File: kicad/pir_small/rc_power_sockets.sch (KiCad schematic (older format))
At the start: 26 parts, among them IC1 ATTINY85, J1 PIR, J2 433MHZ, P1 ICSP, P2 ALT_PWR, Q1 NMOS, Q2 PMOS, SW1 SWITCH_INV, U1 MCP1755ST-3302E/DB

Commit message: Changed layout
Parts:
- removed RV1: POT, Pin_Headers:Pin_Header_Straight_1x03, symbol POT-RESCUE-rc_power_sockets
- added P3, P4: CONN_01X01, theapi_footprints:SMD_PAD, symbol CONN_01X01
- D1, D2, D3: footprint theapi_footprints:SOD-123-Schottky -> theapi_footprints:SOD-123-handsolder
- IC1: footprint theapi_footprints:SOIC-8-N-hand-sold -> theapi_footprints:SOIC-8-N-handsolder
- P2: footprint Pin_Headers:Pin_Header_Straight_1x02 -> Socket_Strips:Socket_Strip_Straight_1x02
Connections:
- net 3.3v: now also P4.1 (P1)
- net ADC3: now also P3.1 (P1)
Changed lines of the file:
@@
 F 0 "IC1" H 5100 5700 50  0000 C CNN
 F 1 "ATTINY85" H 7250 4900 50  0000 C CNN
-F 2 "theapi_footprints:SOIC-8-N-hand-sold" H 7200 5300 50  0000 C CIN
+F 2 "theapi_footprints:SOIC-8-N-handsolder" H 7200 5300 50  0000 C CIN
 F 3 "" H 6250 5300 50  0000 C CNN
 	1    6250 5300
 	1    0    0    -1
 $EndComp
-$Comp
-L POT-RESCUE-rc_power_sockets RV1
-U 1 1 56E809B9
-P 9350 5050
-F 0 "RV1" H 9350 4970 50  0000 C CNN
-F 1 "POT" H 9350 5050 50  0000 C CNN
-F 2 "Pin_Headers:Pin_Header_Straight_1x03" H 9350 5050 50  0001 C CNN
-F 3 "" H 9350 5050 50  0000 C CNN
-	1    9350 5050
-	0    -1   -1   0
-$EndComp
-$Comp
-L GND #PWR08
-U 1 1 56E80AFC
-P 9350 5200
-F 0 "#PWR08" H 9350 4950 50  0001 C CNN
-F 1 "GND" H 9350 5050 50  0000 C CNN
-F 2 "" H 9350 5200 50  0000 C CNN
-F 3 "" H 9350 5200 50  0000 C CNN
-	1    9350 5200
-	1    0    0    -1
-$EndComp
 Text Label 4300 5350 0    60   ~ 0
-ADC3
-Text Label 8900 5050 0    60   ~ 0
 ADC3
 $Comp
@@
 Connection ~ 8250 5050
 Wire Wire Line
-	9200 5050 8900 5050
-Wire Wire Line
-	4900 5350 4300 5350
+	4900 5350 3600 5350
 Connection ~ 6550 3450
 Wire Wire Line
@@
 F 0 "D1" H 4150 3000 50  0000 C CNN
 F 1 "D_Schottky" V 4150 2600 50  0000 C CNN
-F 2 "theapi_footprints:SOD-123-Schottky" H 4150 2900 50  0001 C CNN
+F 2 "theapi_footprints:SOD-123-handsolder" H 4150 2900 50  0001 C CNN
 F 3 "" H 4150 2900 50  0000 C CNN
 	1    4150 2900
@@
 F 0 "D2" H 4150 3350 50  0000 C CNN
 F 1 "D_Schottky" V 4150 3750 50  0000 C CNN
-F 2 "theapi_footprints:SOD-123-Schottky" H 4150 3450 50  0001 C CNN
+F 2 "theapi_footprints:SOD-123-handsolder" H 4150 3450 50  0001 C CNN
 F 3 "" H 4150 3450 50  0000 C CNN
 	1    4150 3450
@@
 F 0 "D3" H 5550 1550 50  0000 C CNN
 F 1 "D_Schottky" V 5550 1950 50  0000 C CNN
-F 2 "theapi_footprints:SOD-123-Schottky" H 5550 1650 50  0001 C CNN
+F 2 "theapi_footprints:SOD-123-handsolder" H 5550 1650 50  0001 C CNN
 F 3 "" H 5550 1650 50  0000 C CNN
 	1    5550 1650
@@
 Wire Wire Line
 	4100 5950 4100 5850
-Wire Wire Line
-	9350 4900 9350 4750
 Wire Wire Line
 	9350 4750 8600 4750
@@
 	2150 5050 1900 5050
 $Comp
-L GND #PWR09
+L GND #PWR08
 U 1 1 56F5DB12
 P 1500 5200
-F 0 "#PWR09" H 1500 4950 50  0001 C CNN
+F 0 "#PWR08" H 1500 4950 50  0001 C CNN
 F 1 "GND" H 1500 5050 50  0000 C CNN
 F 2 "" H 1500 5200 50  0000 C CNN
@@
 Connection ~ 7350 4050
 $Comp
-L GND #PWR010
+L GND #PWR09
 U 1 1 56F7F83F
 P 8600 1050
-F 0 "#PWR010" H 8600 800 50  0001 C CNN
+F 0 "#PWR09" H 8600 800 50  0001 C CNN
 F 1 "GND" H 8600 900 50  0000 C CNN
 F 2 "" H 8600 1050 50  0000 C CNN
@@
 F 0 "P2" H 8800 1150 50  0000 C CNN
 F 1 "ALT_PWR" H 9050 1000 50  0000 C CNN
-F 2 "Pin_Headers:Pin_Header_Straight_1x02" H 8800 1000 50  0001 C CNN
+F 2 "Socket_Strips:Socket_Strip_Straight_1x02" H 8800 1000 50  0001 C CNN
 F 3 "" H 8800 1000 50  0000 C CNN
 	1    8800 1000
@@
 $EndComp
 $Comp
-L GND #PWR011
+L GND #PWR010
 U 1 1 56F8174A
 P 1100 2100
-F 0 "#PWR011" H 1100 1850 50  0001 C CNN
+F 0 "#PWR010" H 1100 1850 50  0001 C CNN
 F 1 "GND" H 1100 1950 50  0000 C CNN
 F 2 "" H 1100 2100 50  0000 C CNN
@@
 $EndComp
 $Comp
-L GND #PWR012
+L GND #PWR011
 U 1 1 56F817AF
 P 1550 2100
-F 0 "#PWR012" H 1550 1850 50  0001 C CNN
+F 0 "#PWR011" H 1550 1850 50  0001 C CNN
 F 1 "GND" H 1550 1950 50  0000 C CNN
 F 2 "" H 1550 2100 50  0000 C CNN
@@
 	6700 850  6550 850
 $Comp
-L GND #PWR013
+L GND #PWR012
 U 1 1 56FBCCBF
 P 6550 1050
-F 0 "#PWR013" H 6550 800 50  0001 C CNN
+F 0 "#PWR012" H 6550 800 50  0001 C CNN
 F 1 "GND" H 6550 900 50  0000 C CNN
 F 2 "" H 6550 1050 50  0000 C CNN
@@
 $EndComp
 $Comp
-L GND #PWR014
+L GND #PWR013
 U 1 1 5722073A
 P 1100 2750
-F 0 "#PWR014" H 1100 2500 50  0001 C CNN
+F 0 "#PWR013" H 1100 2500 50  0001 C CNN
 F 1 "GND" H 1100 2600 50  0000 C CNN
 F 2 "" H 1100 2750 50  0000 C CNN
@@
 $EndComp
 $Comp
-L GND #PWR015
+L GND #PWR014
 U 1 1 57220740
 P 1550 2750
-F 0 "#PWR015" H 1550 2500 50  0001 C CNN
+F 0 "#PWR014" H 1550 2500 50  0001 C CNN
 F 1 "GND" H 1550 2600 50  0000 C CNN
 F 2 "" H 1550 2750 50  0000 C CNN
@@
 	1    0    0    -1
 $EndComp
+$Comp
+L CONN_01X01 P4
+U 1 1 57266A41
+P 9550 4750
+F 0 "P4" H 9550 4850 50  0000 C CNN
+F 1 "CONN_01X01" V 9650 4750 50  0000 C CNN
+F 2 "theapi_footprints:SMD_PAD" H 9550 4750 50  0001 C CNN
+F 3 "" H 9550 4750 50  0000 C CNN
+	1    9550 4750
+	1    0    0    -1
+$EndComp
+$Comp
+L CONN_01X01 P3
+U 1 1 57266AA6
+P 3400 5350
+F 0 "P3" H 3400 5450 50  0000 C CNN
+F 1 "CONN_01X01" V 3500 5350 50  0000 C CNN
+F 2 "theapi_footprints:SMD_PAD" H 3400 5350 50  0001 C CNN
+F 3 "" H 3400 5350 50  0000 C CNN
+	1    3400 5350
+	-1   0    0    1
+$EndComp
 $EndSCHEMATC

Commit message: Silkscreen
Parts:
- P3, P4: footprint theapi_footprints:SMD_PAD -> Pin_Headers:Pin_Header_Straight_1x01
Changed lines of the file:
@@
+$EndComp
+$Comp
+L CONN_01X01 P3
+U 1 1 57266AA6
+P 3400 5350
+F 0 "P3" H 3400 5450 50  0000 C CNN
+F 1 "CONN_01X01" V 3500 5350 50  0000 C CNN
+F 2 "Pin_Headers:Pin_Header_Straight_1x01" H 3400 5350 50  0001 C CNN
+F 3 "" H 3400 5350 50  0000 C CNN
+	1    3400 5350
+	-1   0    0    1
 $EndComp
 $Comp
@@
 F 0 "P4" H 9550 4850 50  0000 C CNN
 F 1 "CONN_01X01" V 9650 4750 50  0000 C CNN
-F 2 "theapi_footprints:SMD_PAD" H 9550 4750 50  0001 C CNN
+F 2 "Pin_Headers:Pin_Header_Straight_1x01" H 9550 4750 50  0001 C CNN
 F 3 "" H 9550 4750 50  0000 C CNN
 	1    9550 4750
 	1    0    0    -1
 $EndComp
-$Comp
-L CONN_01X01 P3
-U 1 1 57266AA6
-P 3400 5350
-F 0 "P3" H 3400 5450 50  0000 C CNN
-F 1 "CONN_01X01" V 3500 5350 50  0000 C CNN
-F 2 "theapi_footprints:SMD_PAD" H 3400 5350 50  0001 C CNN
-F 3 "" H 3400 5350 50  0000 C CNN
-	1    3400 5350
-	-1   0    0    1
-$EndComp
 $EndSCHEMATC

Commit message: Power pins
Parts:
- P2: footprint Socket_Strips:Socket_Strip_Straight_1x02 -> Pin_Headers:Pin_Header_Straight_1x02
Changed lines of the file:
@@
 F 0 "P2" H 8800 1150 50  0000 C CNN
 F 1 "ALT_PWR" H 9050 1000 50  0000 C CNN
-F 2 "Socket_Strips:Socket_Strip_Straight_1x02" H 8800 1000 50  0001 C CNN
+F 2 "Pin_Headers:Pin_Header_Straight_1x02" H 8800 1000 50  0001 C CNN
 F 3 "" H 8800 1000 50  0000 C CNN
 	1    8800 1000

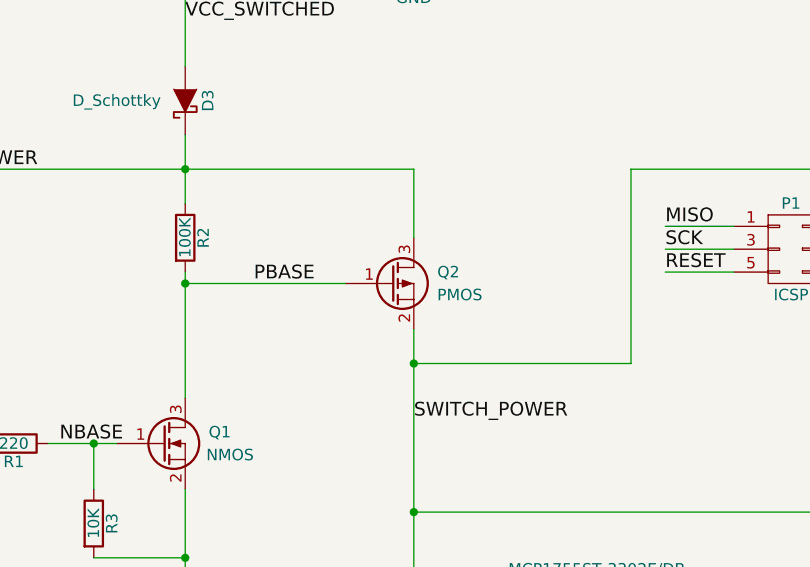
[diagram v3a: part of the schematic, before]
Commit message: Corrected pchannel mosfet
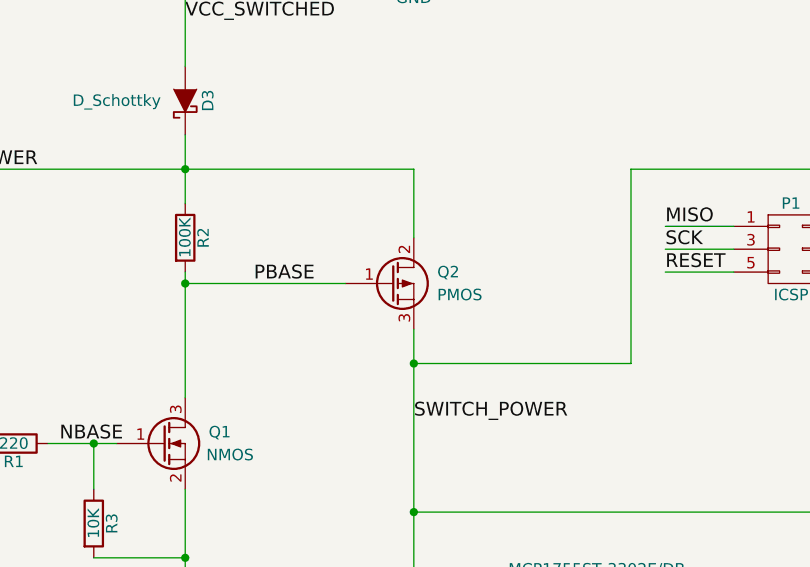
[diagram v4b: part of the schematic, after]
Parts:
- removed Q2: PMOS, TO_SOT_Packages_SMD:SOT-23_Handsoldering, symbol Q_PMOS_GSD
- added Q2: PMOS, TO_SOT_Packages_SMD:SOT-23_Handsoldering, symbol Q_PMOS_GDS
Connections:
- net PBASE: now also Q2.1 (G)
- net POWER: now also Q2.2 (D)
- net SWITCH_POWER: now also Q2.3 (S)
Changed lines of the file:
@@
 ADC3
-$Comp
-L Q_PMOS_GSD Q2
-U 1 1 56E815FA
-P 6450 2450
-F 0 "Q2" H 6750 2500 50  0000 R CNN
-F 1 "PMOS" H 6850 2400 50  0000 R CNN
-F 2 "TO_SOT_Packages_SMD:SOT-23_Handsoldering" H 6650 2550 50  0001 C CNN
-F 3 "" H 6450 2450 50  0000 C CNN
-	1    6450 2450
-	1    0    0    -1
-$EndComp
 $Comp
 L Q_NMOS_GSD Q1
@@
 	1    0    0    -1
 $EndComp
+$Comp
+L Q_PMOS_GDS Q2
+U 1 1 573DB482
+P 6450 2450
+F 0 "Q2" H 6750 2500 50  0000 R CNN
+F 1 "PMOS" H 6850 2400 50  0000 R CNN
+F 2 "TO_SOT_Packages_SMD:SOT-23_Handsoldering" H 6650 2550 50  0001 C CNN
+F 3 "" H 6450 2450 50  0000 C CNN
+	1    6450 2450
+	1    0    0    -1
+$EndComp

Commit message: 10uF cap on the power input
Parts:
- added C4: 10uF, Capacitors_SMD:C_0805_HandSoldering, symbol C
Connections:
- net GND: now also C4.2
- net VCC: now also C4.1
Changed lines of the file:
@@
 Connection ~ 8600 4750
-Wire Wire Line
-	6700 950  8600 950
 Wire Wire Line
 	5550 950  5550 1500
@@
 	1    0    0    -1
 $EndComp
+$Comp
+L C C4
+U 1 1 573F0506
+P 7700 1100
+F 0 "C4" H 7725 1200 50  0000 L CNN
+F 1 "10uF" H 7725 1000 50  0000 L CNN
+F 2 "Capacitors_SMD:C_0805_HandSoldering" H 7738 950 50  0001 C CNN
+F 3 "" H 7700 1100 50  0000 C CNN
+	1    7700 1100
+	1    0    0    -1
+$EndComp
+Wire Wire Line
+	6700 950  8600 950
+Connection ~ 7700 950
+$Comp
+L GND #PWR015
+U 1 1 573F0819
+P 7700 1250
+F 0 "#PWR015" H 7700 1000 50  0001 C CNN
+F 1 "GND" H 7700 1100 50  0000 C CNN
+F 2 "" H 7700 1250 50  0000 C CNN
+F 3 "" H 7700 1250 50  0000 C CNN
+	1    7700 1250
+	1    0    0    -1
+$EndComp
